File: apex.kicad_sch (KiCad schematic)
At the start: 0 parts

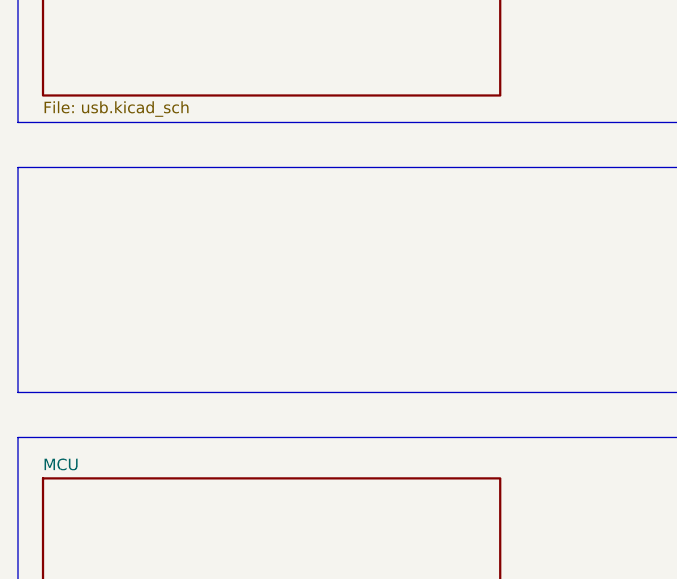
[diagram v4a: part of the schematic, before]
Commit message: separated voltage source labels
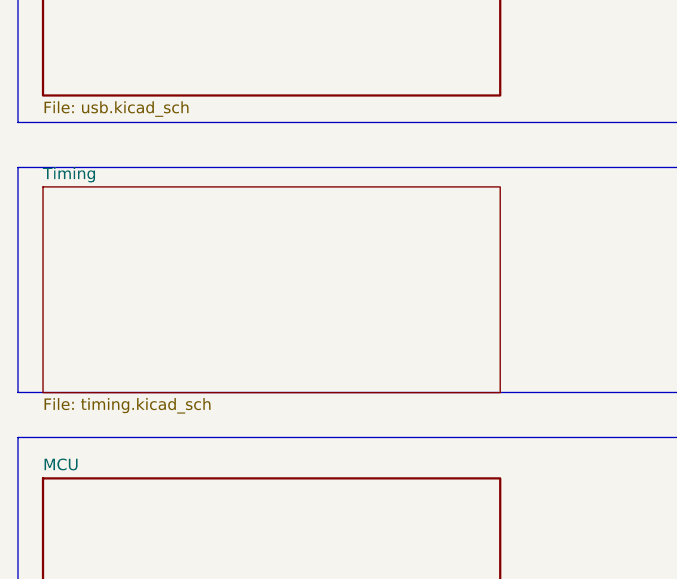
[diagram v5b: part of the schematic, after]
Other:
- added sheet Timing (timing.kicad_sch)
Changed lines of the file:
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@@
+	)
+	(sheet
+		(at 17.78 137.16)
+		(size 50.8 22.86)
+		(fields_autoplaced yes)
+		(stroke
+			(width 0.1524)
+			(type solid)
+		)
+		(fill
+			(color 0 0 0 0.0000)
+		)
+		(property "Sheetname" "Timing"
+			(at 17.78 136.4484 0)
+			(effects
+				(font
+					(size 1.27 1.27)
+				)
+				(justify left bottom)
+			)
+		)
+		(property "Sheetfile" "timing.kicad_sch"
+			(at 17.78 160.6046 0)
+			(effects
+				(font
+					(size 1.27 1.27)
+				)
+				(justify left top)
+			)
+		)
+		(instances
+			(project "apex"
+				(path "/84b8b555-aaa5-476b-b0f2-2d0f894bf0e6"
+					(page "7")
+				)
+			)
+		)
 	)
 	(sheet
